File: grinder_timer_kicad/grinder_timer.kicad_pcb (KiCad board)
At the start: 2 copper layers, 29 parts, among them IC1 ATMEGA328P-P, T1 TRANS, U1 SSD1306_128x64OLED, U2 serial_to_usb, U3 LM7805CT

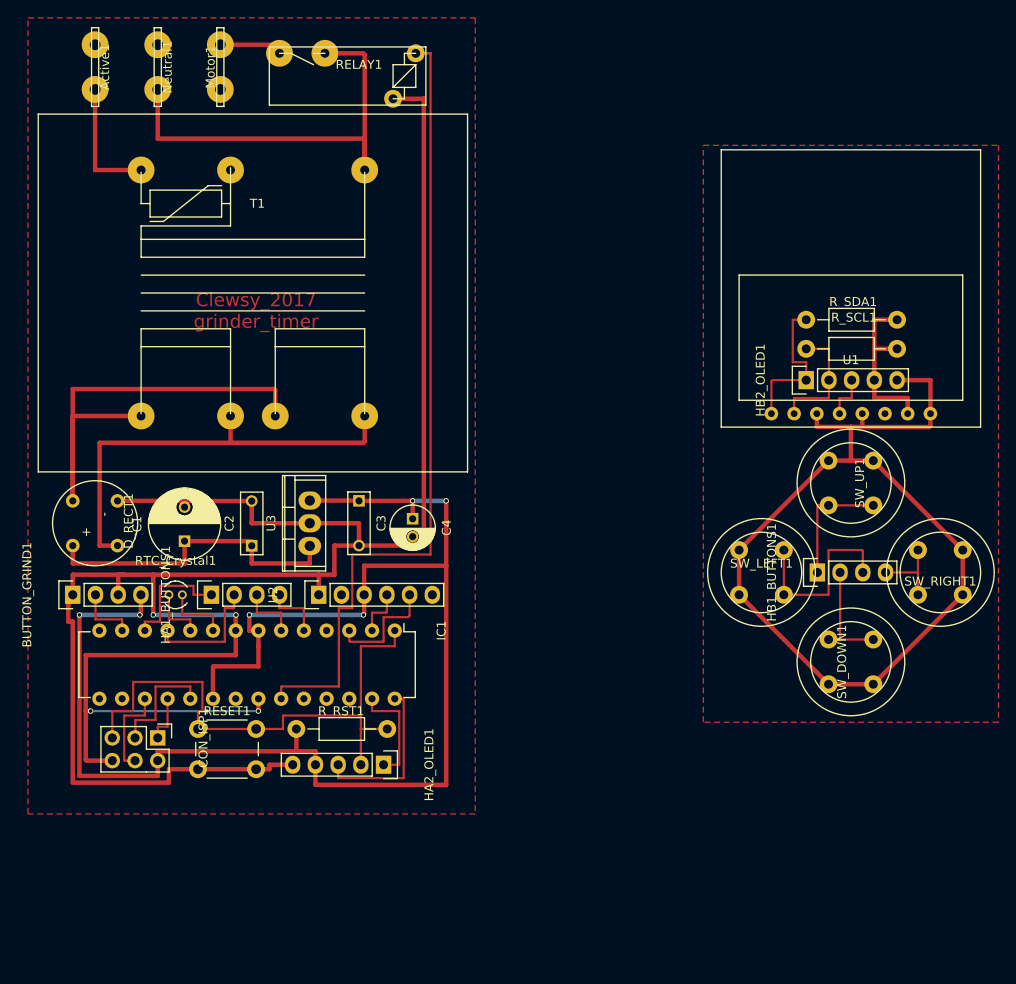
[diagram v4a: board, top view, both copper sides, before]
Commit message: First prototype PCB fabricated and somewhat successful.  Major revision to improve.
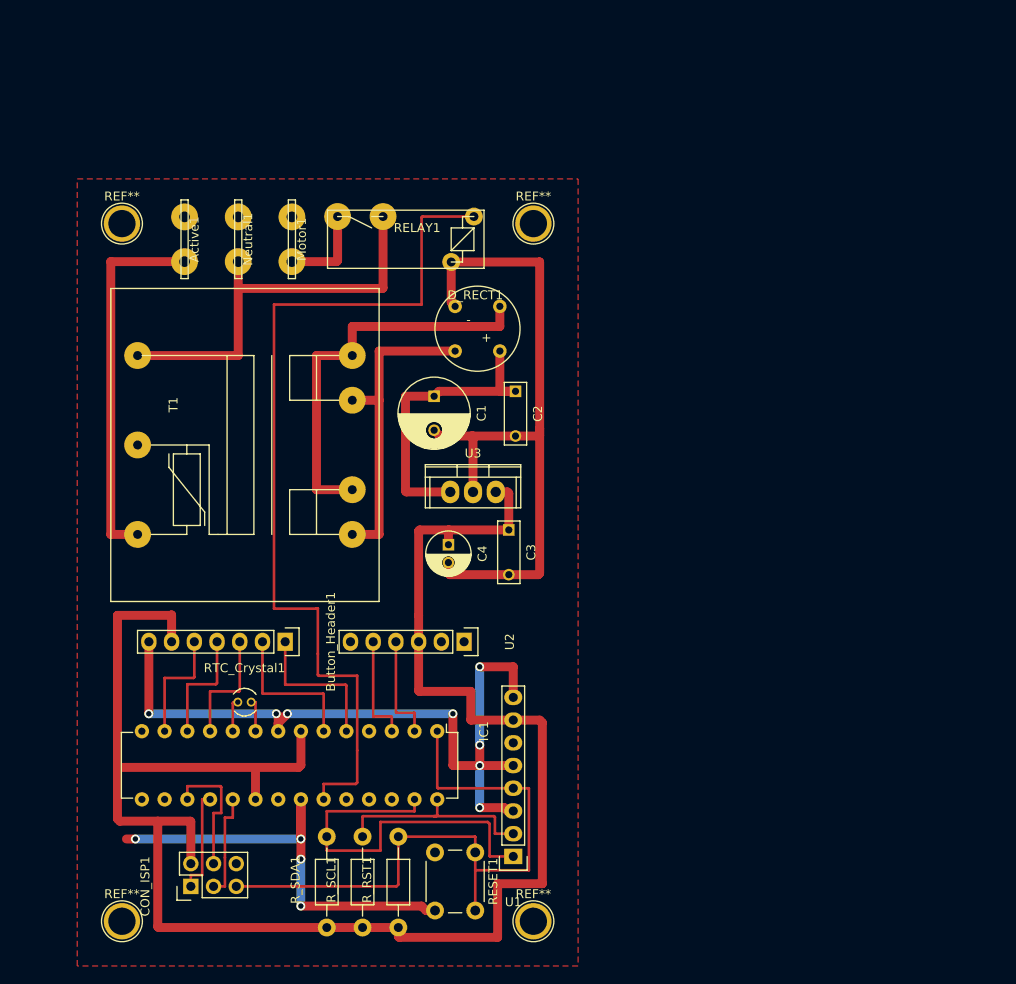
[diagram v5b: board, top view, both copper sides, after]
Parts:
- removed BUTTON_GRIND1: SW_Push_LED, Pin_Headers:Pin_Header_Straight_1x04
- removed HA1_BUTTONS1, HB1_BUTTONS1: CONN_01X04, Pin_Headers:Pin_Header_Straight_1x04
- removed HA2_OLED1, HB2_OLED1: CONN_01X05, Pin_Headers:Pin_Header_Straight_1x05
- removed SW_DOWN1, SW_LEFT1, SW_RIGHT1, SW_UP1: SW_Push_Dual, grinder_timer:TACT
- added Button_Header1: CONN_01X07, Pin_Headers:Pin_Header_Straight_1x07, F.Cu at (83.8, 107.2)
- added REF**: 1pin, Connectors:1pin, F.Cu at (65.5, 60.5)
- added REF**: 1pin, Connectors:1pin, F.Cu at (111.5, 60.5)
- added REF**: 1pin, Connectors:1pin, F.Cu at (65.5, 138.5)
- added REF**: 1pin, Connectors:1pin, F.Cu at (111.5, 138.5)
- U1: footprint grinder_timer:OLED -> Pin_Headers:Pin_Header_Straight_1x08
- moved R_SDA1 86.5 mm to (88.4, 139.2), turned to 90 degrees
- moved R_SCL1 81.5 mm to (92.4, 139.2), turned to 90 degrees
- moved U1 62.3 mm to (109.2, 131.2), turned to 180 degrees
- moved D_RECT1 48.0 mm to (105.2, 72.2), turned to 180 degrees
- moved T1 44.4 mm to (64.2, 67.8), turned to 270 degrees
- moved C2 34.2 mm to (109.5, 79.2), turned to 270 degrees
- moved RESET1 33.9 mm to (105.0, 130.8), turned to 270 degrees
- moved C1 32.3 mm to (100.4, 79.8), turned to 270 degrees
- moved R_RST1 25.0 mm to (96.4, 139.2), turned to 90 degrees
- moved Active1 21.7 mm to (72.5, 62.2)
- moved Neutral1 21.2 mm to (78.5, 62.2)
- moved Motor1 20.8 mm to (84.5, 62.2), turned to 90 degrees
- moved RELAY1 19.4 mm to (98.5, 62.2)
- moved U3 18.6 mm to (104.8, 90.5), turned to 0 degrees
- moved U2 17.1 mm to (103.8, 107.2), turned to 270 degrees
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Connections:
- CON_ISP1 pad 5: HA2_RESET -> RESET
- IC1 pad 1: HA2_RESET -> RESET
- IC1 pad 11: HA1_BUTTON_DOWN -> Net-(Button_Header1-Pad3)
- IC1 pad 12: HA1_BUTTON_UP -> Net-(Button_Header1-Pad4)
- IC1 pad 13: BUTTON_GRIND -> Net-(Button_Header1-Pad5)
- IC1 pad 27: HA2_SDA -> SDA
- IC1 pad 28: HA2_SCL -> SCL
- IC1 pad 5: HA1_BUTTON_RIGHT -> Net-(Button_Header1-Pad1)
- IC1 pad 6: HA1_BUTTON_LEFT -> Net-(Button_Header1-Pad2)
- RESET1 pad 1: HA2_RESET -> RESET
- R_RST1 pad 2: HA2_RESET -> RESET
- R_SCL1 pad 1: HB2_SCL -> +5V
- R_SCL1 pad 2: +5VD -> SCL
- R_SDA1 pad 1: HB2_SDA -> +5V
- R_SDA1 pad 2: +5VD -> SDA
- T1 pad 1: Net-(Neutral1-Pad1) -> Net-(Active1-Pad1)
- T1 pad 3: Net-(Active1-Pad1) -> Net-(T1-Pad3)
- T1 pad 5: Net-(D_RECT1-Pad4) -> Net-(Neutral1-Pad1)
- U1 pad 1: HB2_SDA -> SDA
- U1 pad 2: HB2_SCL -> SCL
- U1 pad 3: GNDD -> GND
- U1 pad 4: HB2_RESET -> RESET
- U1 pad 5: GNDD -> GND
- U1 pad 7: +5VD -> +5V
- U1 pad 8: GNDD -> GND
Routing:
- net GNDD: track 104.9 -> 0.00 mm
- net RESET: track 0.00 -> 72.1 mm
- net HA2_RESET: track 63.5 -> 0.00 mm
- net SDA: track 0.00 -> 43.3 mm
- net GND: track 256.8 -> 216.5 mm, vias 4 -> 12
- net +5V: track 168.9 -> 205.2 mm, vias 6 -> 0
- net Net-(Active1-Pad1): track 14.1 -> 41.8 mm
- net SCL: track 0.00 -> 23.2 mm
- net Net-(HB1_BUTTONS1-Pad3): track 21.3 -> 0.00 mm
- net Net-(D_RECT1-Pad4): track 55.2 -> 35.0 mm
- net +5VD: track 19.3 -> 0.00 mm
- net HA2_SCL: track 18.7 -> 0.00 mm
- net HB2_SDA: track 17.3 -> 0.00 mm
- net Net-(Button_Header1-Pad2): track 0.00 -> 16.8 mm
- net Net-(Button_Header1-Pad1): track 0.00 -> 16.8 mm
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- removed copper zone on F.Cu, net GNDD
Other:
- net class Default: clearance 0.2 -> 0.25; trace_width 0.25 -> 0.3
- net class Power: clearance 0.2 -> 0.25; trace_width 0.5 -> 1; via_dia 0.6 -> 1; via_drill 0.4 -> 0.6
- rule pad_to_mask_clearance: 0.2 -> 0
- rule trace_clearance: 0.2 -> 0.25
- board text removed: "Clewsy_2017 grinder_timer"

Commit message: Tidied schematic and pcb border.
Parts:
- moved Active1 61.5 mm to (134.0, 60.5)
- moved Button_Header1 61.5 mm to (145.2, 105.5)
- moved C1 61.5 mm to (161.9, 78.0)
- moved C2 61.5 mm to (171.0, 77.5)
- moved C3 61.5 mm to (170.2, 93.0)
- moved C4 61.5 mm to (163.5, 94.7)
- moved D_RECT1 61.5 mm to (166.8, 70.5)
- moved IC1 61.5 mm to (162.2, 115.5)
- moved Motor1 61.5 mm to (146.0, 60.5)
- moved Neutral1 61.5 mm to (140.0, 60.5)
- moved REF** 61.5 mm to (127.0, 58.8)
- moved REF** 61.5 mm to (173.0, 58.8)
- moved REF** 61.5 mm to (127.0, 136.8)
- moved REF** 61.5 mm to (173.0, 136.8)
- moved RELAY1 61.5 mm to (160.0, 60.5)
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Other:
- board text added: "04/12/2017"
- board text added: "grinder_timer"
- board text added: "refer to https://github.com/Clewsy/grinder_timer"
